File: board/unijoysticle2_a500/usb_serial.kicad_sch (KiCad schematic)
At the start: 12 parts, among them J1 USB_B_Micro, U2 AMS1117-3.3, U3 CH340C

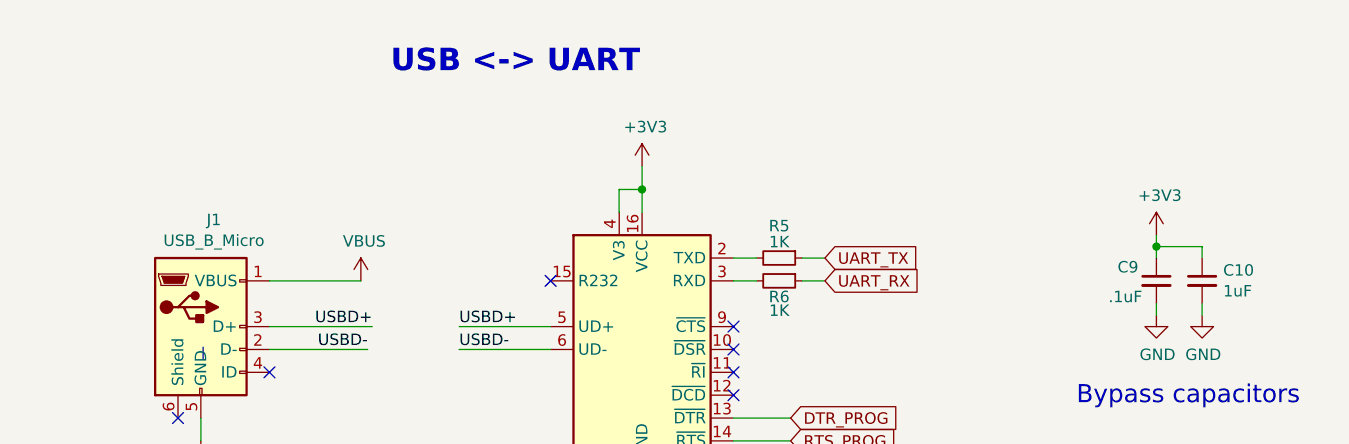
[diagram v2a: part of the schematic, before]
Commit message: Uni2 A500: CH340 powered by VBUS
Instead of powering CH340 from V3, power it from VBUS.
This should help, when the device is powered by the Amiga, it should not
power the CH340.

Not tested.
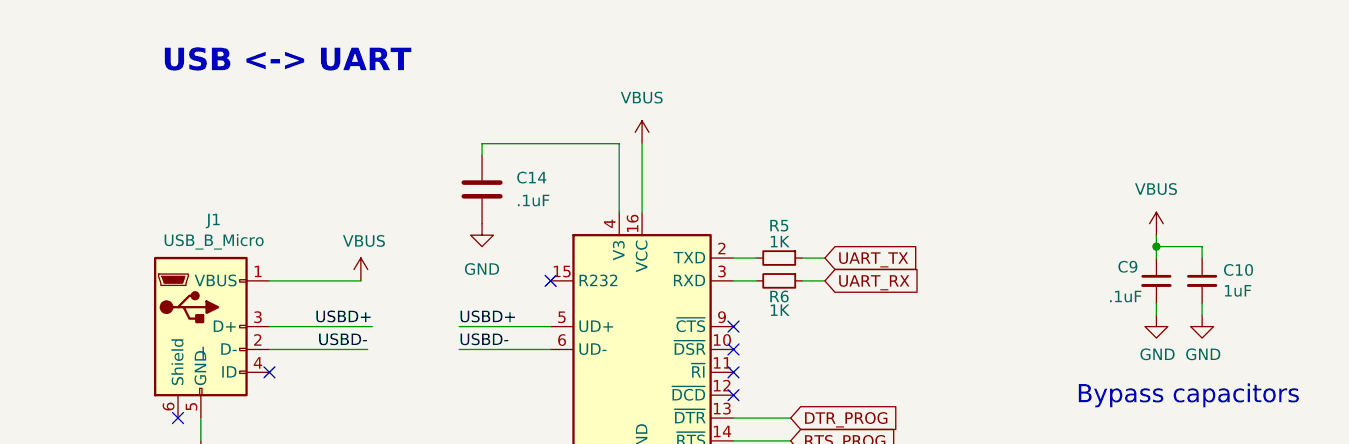
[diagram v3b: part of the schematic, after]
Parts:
- added C14: .1uF, Capacitor_SMD:C_0805_2012Metric_Pad1.18x1.45mm_HandSolder, symbol Device:C
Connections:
- net +3V3: no longer C10.1, C9.1, U3.16 (VCC), U3.4 (V3)
- net GND: now also C14.2
- net VBUS: now also C10.1, C9.1, U3.16 (VCC)
- new net: C14.1, U3.4 (V3)
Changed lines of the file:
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@@
     (company "Retro Moe")
-  )
-  (junction (at 194.31 31.75) (diameter 0) (color 0 0 0 0)
   )
   (junction (at 60.96 48.26) (diameter 0) (color 0 0 0 0)
@@
     (stroke (width 0) (type default) (color 0 0 0 0))
   )
-  (wire (pts (xy 194.31 31.75) (xy 194.31 34.29))
+  (wire (pts (xy 176.53 26.67) (xy 176.53 27.94))
     (stroke (width 0) (type default) (color 0 0 0 0))
   )
@@
     (stroke (width 0) (type default) (color 0 0 0 0))
   )
-  (wire (pts (xy 191.77 31.75) (xy 191.77 34.29))
+  (wire (pts (xy 191.77 34.29) (xy 191.77 26.67))
     (stroke (width 0) (type default) (color 0 0 0 0))
   )
@@
     (stroke (width 0) (type default) (color 0 0 0 0))
   )
-  (wire (pts (xy 194.31 29.21) (xy 194.31 31.75))
+  (wire (pts (xy 191.77 26.67) (xy 176.53 26.67))
     (stroke (width 0) (type default) (color 0 0 0 0))
   )
@@
     (stroke (width 0) (type default) (color 0 0 0 0))
   )
-  (wire (pts (xy 194.31 31.75) (xy 191.77 31.75))
-    (stroke (width 0) (type default) (color 0 0 0 0))
-  )
   (polyline (pts (xy 113.03 12.7) (xy 113.03 102.87))
     (stroke (width 0) (type default) (color 0 0 0 0))
@@
   )
   (polyline (pts (xy 113.03 102.87) (xy 284.48 102.87))
+    (stroke (width 0) (type default) (color 0 0 0 0))
+  )
+  (wire (pts (xy 194.31 26.67) (xy 194.31 34.29))
     (stroke (width 0) (type default) (color 0 0 0 0))
   )
@@
     (effects (font (size 2 2)) (justify left bottom))
   )
-  (text "USB <-> UART" (at 166.37 19.05 0)
+  (text "USB <-> UART" (at 140.97 19.05 0)
     (effects (font (size 2.4892 2.4892) (thickness 0.4978) bold) (justify left bottom))
   )
@@
     (pin "2")
   )
-  (symbol (lib_id "power:+3V3") (at 194.31 29.21 0) (unit 1)
-    (in_bom yes) (on_board yes)
-    (property "Reference" "#PWR020" (id 0) (at 194.31 33.02 0)
-      (effects (font (size 1.27 1.27)) hide)
-    )
-    (property "Value" "+3V3" (id 1) (at 194.691 24.8158 0))
-    (property "Footprint" "" (id 2) (at 194.31 29.21 0)
-      (effects (font (size 1.27 1.27)) hide)
-    )
-    (property "Datasheet" "" (id 3) (at 194.31 29.21 0)
-      (effects (font (size 1.27 1.27)) hide)
-    )
-    (pin "1")
-  )
   (symbol (lib_id "power:GND") (at 194.31 67.31 0) (unit 1)
     (in_bom yes) (on_board yes)
@@
     )
     (property "Datasheet" "" (id 3) (at 194.31 67.31 0)
-      (effects (font (size 1.27 1.27)) hide)
-    )
-    (pin "1")
-  )
-  (symbol (lib_id "power:+3V3") (at 251.46 36.83 0) (unit 1)
-    (in_bom yes) (on_board yes)
-    (property "Reference" "#PWR022" (id 0) (at 251.46 40.64 0)
-      (effects (font (size 1.27 1.27)) hide)
-    )
-    (property "Value" "+3V3" (id 1) (at 251.841 32.4358 0))
-    (property "Footprint" "" (id 2) (at 251.46 36.83 0)
-      (effects (font (size 1.27 1.27)) hide)
-    )
-    (property "Datasheet" "" (id 3) (at 251.46 36.83 0)
       (effects (font (size 1.27 1.27)) hide)
     )
@@
     (pin "1")
   )
+  (symbol (lib_id "power:VBUS") (at 251.46 36.83 0) (unit 1)
+    (in_bom yes) (on_board yes) (fields_autoplaced)
+    (property "Reference" "#PWR0102" (id 0) (at 251.46 40.64 0)
+      (effects (font (size 1.27 1.27)) hide)
+    )
+    (property "Value" "VBUS" (id 1) (at 251.46 31.75 0))
+    (property "Footprint" "" (id 2) (at 251.46 36.83 0)
+      (effects (font (size 1.27 1.27)) hide)
+    )
+    (property "Datasheet" "" (id 3) (at 251.46 36.83 0)
+      (effects (font (size 1.27 1.27)) hide)
+    )
+    (pin "1")
+  )
   (symbol (lib_id "power:PWR_FLAG") (at 64.77 44.45 0) (unit 1)
     (in_bom yes) (on_board yes) (fields_autoplaced)
@@
     (pin "1")
   )
+  (symbol (lib_id "power:VBUS") (at 194.31 26.67 0) (unit 1)
+    (in_bom yes) (on_board yes) (fields_autoplaced)
+    (property "Reference" "#PWR0101" (id 0) (at 194.31 30.48 0)
+      (effects (font (size 1.27 1.27)) hide)
+    )
+    (property "Value" "VBUS" (id 1) (at 194.31 21.59 0))
+    (property "Footprint" "" (id 2) (at 194.31 26.67 0)
+      (effects (font (size 1.27 1.27)) hide)
+    )
+    (property "Datasheet" "" (id 3) (at 194.31 26.67 0)
+      (effects (font (size 1.27 1.27)) hide)
+    )
+    (pin "1")
+  )
+  (symbol (lib_id "power:GND") (at 176.53 35.56 0) (unit 1)
+    (in_bom yes) (on_board yes) (fields_autoplaced)
+    (property "Reference" "#PWR0103" (id 0) (at 176.53 41.91 0)
+      (effects (font (size 1.27 1.27)) hide)
+    )
+    (property "Value" "GND" (id 1) (at 176.53 40.64 0))
+    (property "Footprint" "" (id 2) (at 176.53 35.56 0)
+      (effects (font (size 1.27 1.27)) hide)
+    )
+    (property "Datasheet" "" (id 3) (at 176.53 35.56 0)
+      (effects (font (size 1.27 1.27)) hide)
+    )
+    (pin "1")
+  )
   (symbol (lib_id "Device:C_Polarized_Small") (at 53.34 53.34 0) (unit 1)
     (in_bom yes) (on_board yes)
@@
       (effects (font (size 1.27 1.27)) hide)
     )
+    (pin "1")
+    (pin "2")
+  )
+  (symbol (lib_id "Device:C") (at 176.53 31.75 0) (unit 1)
+    (in_bom yes) (on_board yes) (fields_autoplaced)
+    (property "Reference" "C14" (id 0) (at 180.34 30.4799 0)
+      (effects (font (size 1.27 1.27)) (justify left))
+    )
+    (property "Value" ".1uF" (id 1) (at 180.34 33.0199 0)
+      (effects (font (size 1.27 1.27)) (justify left))
+    )
+    (property "Footprint" "Capacitor_SMD:C_0805_2012Metric_Pad1.18x1.45mm_HandSolder" (id 2) (at 177.4952 35.56 0)
+      (effects (font (size 1.27 1.27)) hide)
+    )
+    (property "Datasheet" "~" (id 3) (at 176.53 31.75 0)
+      (effects (font (size 1.27 1.27)) hide)
+    )

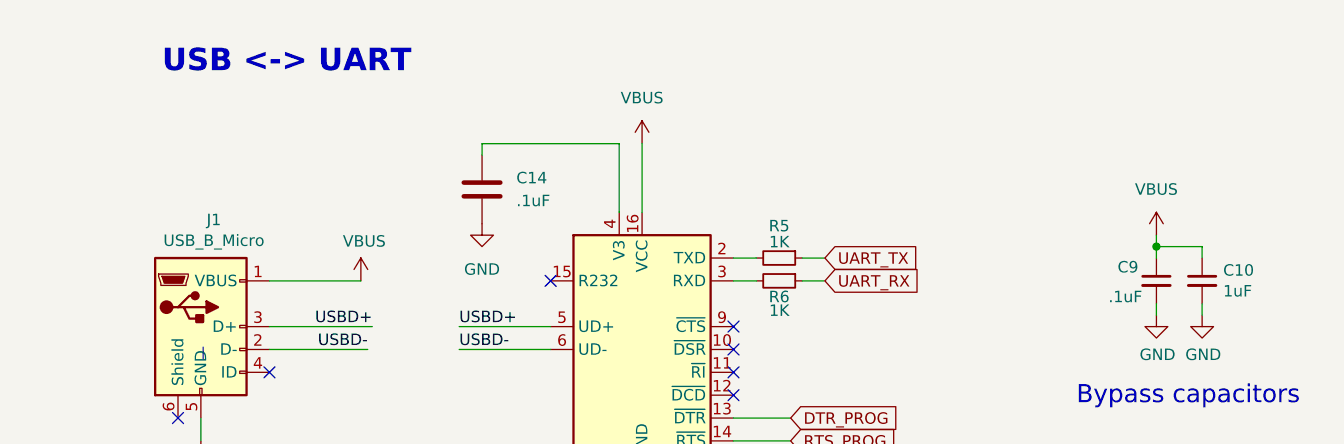
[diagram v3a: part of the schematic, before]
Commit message: uni2 a500: revert CH340 from 5V
Autoreset is driven by DTS/RTS.
But if DTS/RTS are not used (requires that CH340 is powered) then
autoreset doesn't work.
So, although we shouldn't power CH340 when it is powered from the Amiga,
since it consumes current, we need it for autoreset.

Besides, we don't gain much by not powering CH340. Only 0.02 amps
according to my measures.
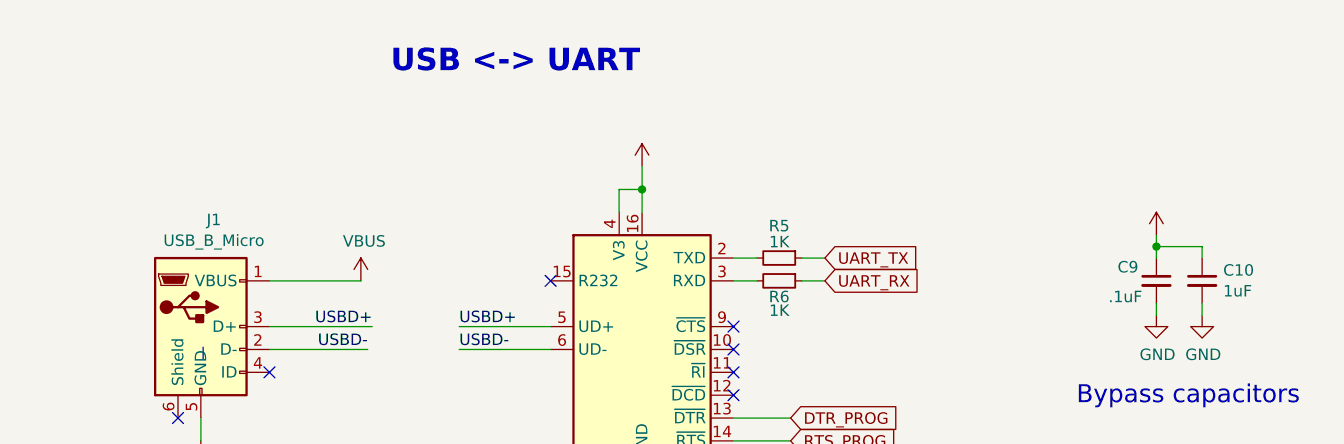
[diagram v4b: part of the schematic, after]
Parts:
- removed C14: .1uF, Capacitor_SMD:C_0805_2012Metric_Pad1.18x1.45mm_HandSolder, symbol Device:C
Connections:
- net +3V3: now also C10.1, C9.1, U3.16 (VCC), U3.4 (V3)
- net VBUS: no longer C10.1, C9.1, U3.16 (VCC)
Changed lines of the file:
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@@
   (title_block
     (title "Unijoysticle 2 A500")
-    (date "2022-05-15")
-    (rev "B")
+    (date "2022-04-25")
+    (rev "A")
     (company "Retro Moe")
+  )
+  (junction (at 194.31 31.75) (diameter 0) (color 0 0 0 0)
   )
   (junction (at 60.96 48.26) (diameter 0) (color 0 0 0 0)
@@
     (stroke (width 0) (type default) (color 0 0 0 0))
   )
-  (wire (pts (xy 176.53 26.67) (xy 176.53 27.94))
+  (wire (pts (xy 194.31 31.75) (xy 194.31 34.29))
     (stroke (width 0) (type default) (color 0 0 0 0))
   )
@@
     (stroke (width 0) (type default) (color 0 0 0 0))
   )
-  (wire (pts (xy 191.77 34.29) (xy 191.77 26.67))
+  (wire (pts (xy 191.77 31.75) (xy 191.77 34.29))
     (stroke (width 0) (type default) (color 0 0 0 0))
   )
@@
     (stroke (width 0) (type default) (color 0 0 0 0))
   )
-  (wire (pts (xy 191.77 26.67) (xy 176.53 26.67))
+  (wire (pts (xy 194.31 29.21) (xy 194.31 31.75))
     (stroke (width 0) (type default) (color 0 0 0 0))
   )
@@
     (stroke (width 0) (type default) (color 0 0 0 0))
   )
+  (wire (pts (xy 194.31 31.75) (xy 191.77 31.75))
+    (stroke (width 0) (type default) (color 0 0 0 0))
+  )
   (polyline (pts (xy 113.03 12.7) (xy 113.03 102.87))
     (stroke (width 0) (type default) (color 0 0 0 0))
@@
   )
   (polyline (pts (xy 113.03 102.87) (xy 284.48 102.87))
-    (stroke (width 0) (type default) (color 0 0 0 0))
-  )
-  (wire (pts (xy 194.31 26.67) (xy 194.31 34.29))
     (stroke (width 0) (type default) (color 0 0 0 0))
   )
@@
     (effects (font (size 2 2)) (justify left bottom))
   )
-  (text "USB <-> UART" (at 140.97 19.05 0)
+  (text "USB <-> UART" (at 166.37 19.05 0)
     (effects (font (size 2.4892 2.4892) (thickness 0.4978) bold) (justify left bottom))
   )
@@
     (pin "2")
   )
+  (symbol (lib_id "power:+3V3") (at 194.31 29.21 0) (unit 1)
+    (in_bom yes) (on_board yes)
+    (property "Reference" "#PWR020" (id 0) (at 194.31 33.02 0)
+      (effects (font (size 1.27 1.27)) hide)
+    )
+    (property "Value" "" (id 1) (at 194.691 24.8158 0))
+    (property "Footprint" "" (id 2) (at 194.31 29.21 0)
+      (effects (font (size 1.27 1.27)) hide)
+    )
+    (property "Datasheet" "" (id 3) (at 194.31 29.21 0)
+      (effects (font (size 1.27 1.27)) hide)
+    )
+    (pin "1")
+  )
   (symbol (lib_id "power:GND") (at 194.31 67.31 0) (unit 1)
     (in_bom yes) (on_board yes)
@@
     )
     (property "Datasheet" "" (id 3) (at 194.31 67.31 0)
+      (effects (font (size 1.27 1.27)) hide)
+    )
+    (pin "1")
+  )
+  (symbol (lib_id "power:+3V3") (at 251.46 36.83 0) (unit 1)
+    (in_bom yes) (on_board yes)
+    (property "Reference" "#PWR022" (id 0) (at 251.46 40.64 0)
+      (effects (font (size 1.27 1.27)) hide)
+    )
+    (property "Value" "" (id 1) (at 251.841 32.4358 0))
+    (property "Footprint" "" (id 2) (at 251.46 36.83 0)
+      (effects (font (size 1.27 1.27)) hide)
+    )
+    (property "Datasheet" "" (id 3) (at 251.46 36.83 0)
       (effects (font (size 1.27 1.27)) hide)
     )
@@
     (pin "1")
   )
-  (symbol (lib_id "power:VBUS") (at 251.46 36.83 0) (unit 1)
-    (in_bom yes) (on_board yes) (fields_autoplaced)
-    (property "Reference" "#PWR0102" (id 0) (at 251.46 40.64 0)
-      (effects (font (size 1.27 1.27)) hide)
-    )
-    (property "Value" "VBUS" (id 1) (at 251.46 31.75 0))
-    (property "Footprint" "" (id 2) (at 251.46 36.83 0)
-      (effects (font (size 1.27 1.27)) hide)
-    )
-    (property "Datasheet" "" (id 3) (at 251.46 36.83 0)
-      (effects (font (size 1.27 1.27)) hide)
-    )
-    (pin "1")
-  )
   (symbol (lib_id "power:PWR_FLAG") (at 64.77 44.45 0) (unit 1)
     (in_bom yes) (on_board yes) (fields_autoplaced)
@@
     (pin "1")
   )
-  (symbol (lib_id "power:VBUS") (at 194.31 26.67 0) (unit 1)
-    (in_bom yes) (on_board yes) (fields_autoplaced)
-    (property "Reference" "#PWR0101" (id 0) (at 194.31 30.48 0)
-      (effects (font (size 1.27 1.27)) hide)
-    )
-    (property "Value" "VBUS" (id 1) (at 194.31 21.59 0))
-    (property "Footprint" "" (id 2) (at 194.31 26.67 0)
-      (effects (font (size 1.27 1.27)) hide)
-    )
-    (property "Datasheet" "" (id 3) (at 194.31 26.67 0)
-      (effects (font (size 1.27 1.27)) hide)
-    )
-    (pin "1")
-  )
-  (symbol (lib_id "power:GND") (at 176.53 35.56 0) (unit 1)
-    (in_bom yes) (on_board yes) (fields_autoplaced)
-    (property "Reference" "#PWR0103" (id 0) (at 176.53 41.91 0)
-      (effects (font (size 1.27 1.27)) hide)
-    )
-    (property "Value" "GND" (id 1) (at 176.53 40.64 0))
-    (property "Footprint" "" (id 2) (at 176.53 35.56 0)
-      (effects (font (size 1.27 1.27)) hide)
-    )
-    (property "Datasheet" "" (id 3) (at 176.53 35.56 0)
-      (effects (font (size 1.27 1.27)) hide)
-    )
-    (pin "1")
-  )
   (symbol (lib_id "Device:C_Polarized_Small") (at 53.34 53.34 0) (unit 1)
     (in_bom yes) (on_board yes)
@@
       (effects (font (size 1.27 1.27)) hide)
     )
-    (pin "1")
-    (pin "2")
-  )
-  (symbol (lib_id "Device:C") (at 176.53 31.75 0) (unit 1)
-    (in_bom yes) (on_board yes) (fields_autoplaced)
-    (property "Reference" "C14" (id 0) (at 180.34 30.4799 0)
-      (effects (font (size 1.27 1.27)) (justify left))
-    )
-    (property "Value" ".1uF" (id 1) (at 180.34 33.0199 0)
-      (effects (font (size 1.27 1.27)) (justify left))
-    )
-    (property "Footprint" "Capacitor_SMD:C_0805_2012Metric_Pad1.18x1.45mm_HandSolder" (id 2) (at 177.4952 35.56 0)
-      (effects (font (size 1.27 1.27)) hide)
-    )
-    (property "Datasheet" "~" (id 3) (at 176.53 31.75 0)
-      (effects (font (size 1.27 1.27)) hide)
-    )

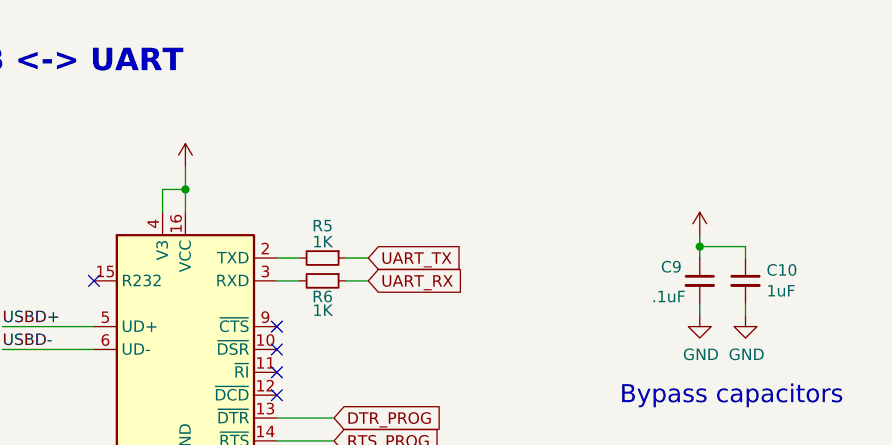
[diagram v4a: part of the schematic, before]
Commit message: uni2 a500: silkscreen improments
mouse -> mode
add copyright
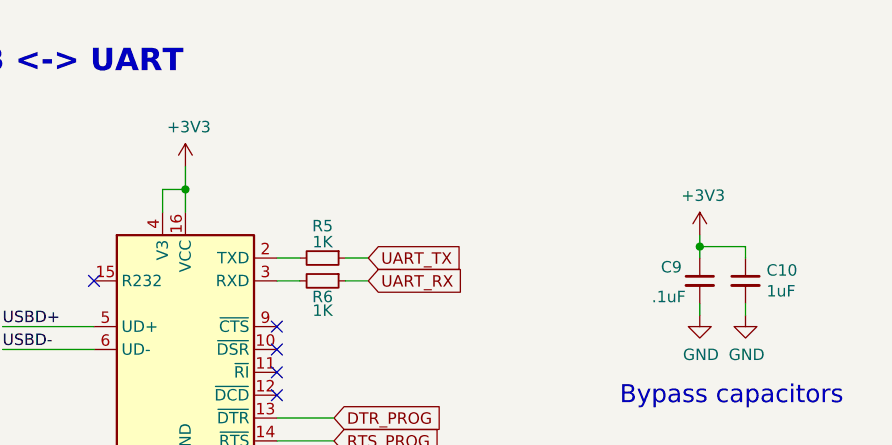
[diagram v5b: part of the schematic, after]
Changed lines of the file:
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@@
       (effects (font (size 1.27 1.27)) hide)
     )
-    (property "Value" "" (id 1) (at 194.691 24.8158 0))
+    (property "Value" "+3V3" (id 1) (at 194.691 24.8158 0))
     (property "Footprint" "" (id 2) (at 194.31 29.21 0)
       (effects (font (size 1.27 1.27)) hide)
@@
       (effects (font (size 1.27 1.27)) hide)
     )
-    (property "Value" "" (id 1) (at 251.841 32.4358 0))
+    (property "Value" "+3V3" (id 1) (at 251.841 32.4358 0))
     (property "Footprint" "" (id 2) (at 251.46 36.83 0)
       (effects (font (size 1.27 1.27)) hide)

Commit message: Uni2 A500: Change company name
from Retro Moe to Ricardo Quesada
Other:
- company: Retro Moe -> Ricardo Quesada
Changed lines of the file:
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@@
     (date "2022-04-25")
     (rev "A")
-    (company "Retro Moe")
+    (company "Ricardo Quesada")
   )
   (junction (at 194.31 31.75) (diameter 0) (color 0 0 0 0)
